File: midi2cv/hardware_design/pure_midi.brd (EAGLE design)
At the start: 78.9 x 100 mm, 92 parts, among them IC1 LD117AS50TR, IC2 74HCT125D, IC3 6N138SMD, IC4 74HCT125D, IC5 STM32F10XCXT6, IC6 LD117AS33TR, J1 CORTEX_DEBUG_PTH, SW1 EC12E_SW, U1 AD5676ARUZ, U2 AD5754BREZ, U3 TEXAS_INSTRUMENTS_LM4040C5IDB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, U4 MAX3421, U5 TEXAS_INSTRUMENTS_LM4040C25ID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, X1 OG-MIDI_MAB5SHCUI-SD-50BV, X2 KUSBVX, X3 OG-MIDI_MAB5SHCUI-SD-50BV, X4 KUSBVX-BS1N, X6 ABRACON_ABM3B-12.000MHZ-B2-TA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, X7 ABRACON_ABM3B-8.000MHZ-B2-TAB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

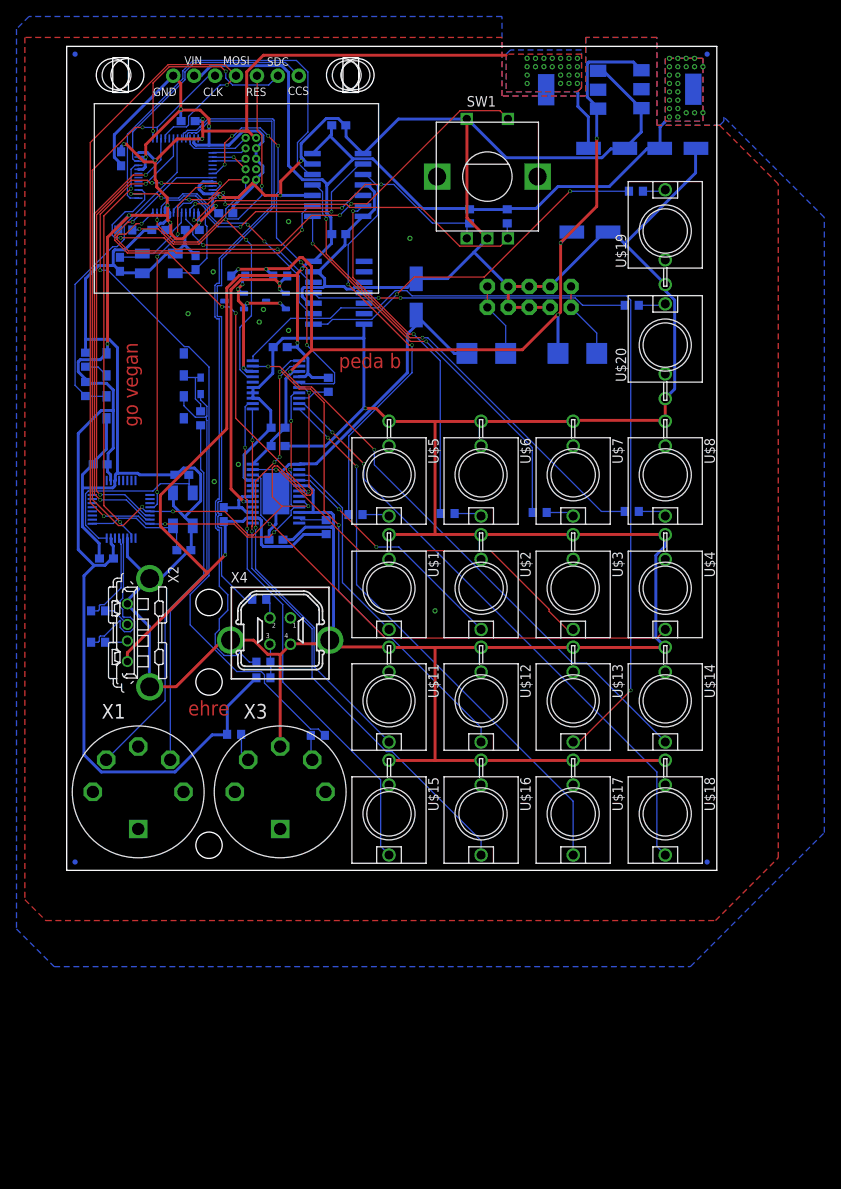
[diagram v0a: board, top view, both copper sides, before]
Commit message: Use newer processor for midi2cv, fix some hardware mistakes
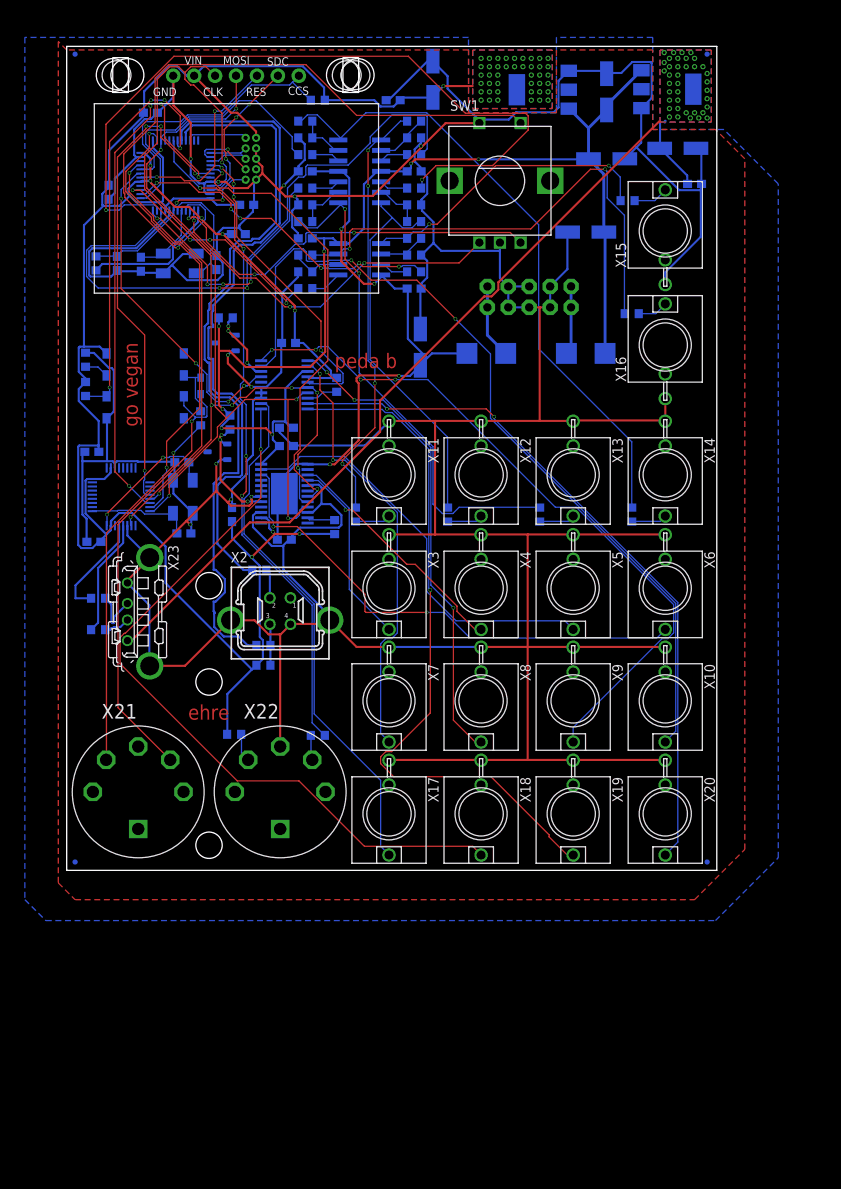
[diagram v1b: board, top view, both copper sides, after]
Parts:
- removed DI1: OLED_1.3_128X64_SPI, microbuilder:C1_ADAFRUIT_1.3_128X64_OLED
- removed U$1, U$11, U$2, U$4: WQP-PJ301M-12_JACK, thonkiconn:WQP-PJ301M-12_JACK
- removed U5: TEXAS_INSTRUMENTS_LM4040C25IDBZRTEXAS_INSTRUMENTS_LM4040C25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, lm4040:TEXAS_INSTRUMENTS_LM4040C25IDBZR_1
- added C18, C19, C20, C22: 22u, GMSN:153CLV-0505
- added C27, C28: 100n, rcl:C0603
- added D4: 1N4001, GMSN:SMADIODE
- added IC7: LD117AS50TR, v-reg:SOT223
- added R22: 33R, rcl:R0603
- added R23, R30, R34, R38: 10k, rcl:R0603
- added R24, R31, R35, R39: 56k, rcl:R0603
- added R25, R28, R32, R36, R40: 39k, rcl:R0603
- added R29, R33, R37: 1k, rcl:R0603
- added X21, X22: OG-MIDI_MAB5SHCUI-SD-50BV, yarns_v03:OG-MIDI_SD-50BV
- added X23: KUSBVX, con-kycon:KUSBVX
- added X24: ABRACON_ABM3B-12.000MHZ-B2-TABRACON_ABM3B-12.000MHZ-B2-T_0_0, Abracon - ABM3B-12.000MHZ-B2-T:ABRACON_ABM3B-12.000MHZ-B2-T_0
- C1, C2, C7, C8: value 22p -> 100n
- C14, C15: value 100n -> 22p
- C21, C23: value 100n -> 22u; device rcl:C0603 -> GMSN:153CLV-0505
- C24, C25: value 100n -> 100nF
- C3, C4: value 22u -> 22p; device GMSN:153CLV-0505 -> rcl:C0603
- C5, C6: value 22u -> 100n; device GMSN:153CLV-0505 -> rcl:C0603
- D1: value 1N4148 -> OLED_1.3_128X64_SPI; device adafruit:SOD-323F -> microbuilder:C1_ADAFRUIT_1.3_128X64_OLED
- D2: value 1N4001 -> 1N4148; device GMSN:SMADIODE -> adafruit:SOD-323F
- IC1: value LD117AS50TR -> STM32F373C; device v-reg:SOT223 -> og-stm32f2:LQFP48
- IC2: value 74HCT125D -> AD5754BREZ; device 74xx-eu:SO14 -> ad5754:RE_24
- IC3: value 6N138SMD -> TL074D; device 6n138:SO8-GW300 -> linear:SO14
- IC4: value 74HCT125D -> TL072D; device 74xx-eu:SO14 -> linear:SO08
- IC5: value STM32F10XCXT6 -> 6N138SMD; device stm32:TQFP48 -> 6n138:SO8-GW300
- R1: value 1k -> 1k5
- R10: value 51R -> 1k
- R11: value 220R -> 1k
- R12: value 470R -> 10k
- R13: value 22R -> 56k
- R14: value 22R -> 39k
- R15: value 10k -> 1k; device resistor:R0603 -> rcl:R0603
- R16: value 10k -> 51R; device resistor:R0603 -> rcl:R0603
- R17: value 1k -> 220R
- R18: value 2k -> 51R
- R19: value 2k -> 1k
- R2, R3: value 4k7 -> 22R
- R20: value 1k5 -> 470R
- R21: value 10k -> 33R
- R26: value 33R -> 10k
- R27: value 33R -> 56k
- R4: value 1k -> 10k
- R5: value 1k -> 10k; device rcl:R0603 -> resistor:R0603
- R6, R7: value 1k -> 4k7
- R8: value 1k -> 2k
- R9: value 51R -> 2k
- U1: value AD5676ARUZ -> TEXAS_INSTRUMENTS_LM4040C5IDBZR1; device AD5676ARUZ:RU_20 -> lm4040:TEXAS_INSTRUMENTS_LM4040C5IDBZR_1
- U2: value AD5754BREZ -> AD5676ARUZ; device ad5754:RE_24 -> AD5676ARUZ:RU_20
- U3: value TEXAS_INSTRUMENTS_LM4040C5IDBZR1 -> TEXAS_INSTRUMENTS_LM4040C25IDBZRTEXAS_INSTRUMENTS_LM4040C25IDBZR_0_1; device lm4040:TEXAS_INSTRUMENTS_LM4040C5IDBZR_1 -> lm4040:TEXAS_INSTRUMENTS_LM4040C25IDBZR_1
- X1: value OG-MIDI_MAB5SHCUI-SD-50BV -> ABRACON_ABM3B-8.000MHZ-B2-TABRACON_ABM3B-8.000MHZ-B2-T_0_0; device yarns_v03:OG-MIDI_SD-50BV -> Abracon - ABM3B-8.000MHZ-B2-T:ABRACON_ABM3B-8.000MHZ-B2-T_0
- X2: value KUSBVX -> KUSBVX-BS1N; device con-kycon:KUSBVX -> con-kycon:KUSBVX-BS1N
- X3: value OG-MIDI_MAB5SHCUI-SD-50BV -> WQP-PJ301M-12_JACK; device yarns_v03:OG-MIDI_SD-50BV -> thonkiconn:WQP-PJ301M-12_JACK
- X4: value KUSBVX-BS1N -> WQP-PJ301M-12_JACK; device con-kycon:KUSBVX-BS1N -> thonkiconn:WQP-PJ301M-12_JACK
- X6: value ABRACON_ABM3B-12.000MHZ-B2-TABRACON_ABM3B-12.000MHZ-B2-T_0_0 -> WQP-PJ301M-12_JACK; device Abracon - ABM3B-12.000MHZ-B2-T:ABRACON_ABM3B-12.000MHZ-B2-T_0 -> thonkiconn:WQP-PJ301M-12_JACK
- X7: value ABRACON_ABM3B-8.000MHZ-B2-TABRACON_ABM3B-8.000MHZ-B2-T_0_0 -> WQP-PJ301M-12_JACK; device Abracon - ABM3B-8.000MHZ-B2-T:ABRACON_ABM3B-8.000MHZ-B2-T_0 -> thonkiconn:WQP-PJ301M-12_JACK
- moved C21 79.9 mm to (74.2, 87.6)
- moved R16 67.1 mm to (30.5, 16.4), turned to 0 degrees
- moved X1 64.3 mm to (13.7, 73.7), flipped to the bottom, turned to 180 degrees
- moved C5 64.2 mm to (10.2, 91.9), turned to 180 degrees
- moved C6 61.1 mm to (6.10, 73.7), turned to 270 degrees
- moved IC1 60.6 mm to (13.2, 84.3), turned to 0 degrees
- moved R26 60.6 mm to (29.0, 82.8)
- moved X7 60.0 mm to (39.1, 20.6), flipped to the top
- moved X6 59.3 mm to (72.6, 34.2), flipped to the top, turned to 180 degrees
- moved R14 58.4 mm to (42.2, 80.8), turned to 180 degrees
- moved C24 57.0 mm to (76.2, 83.3)
- moved R5 56.8 mm to (30.5, 93.5), turned to 180 degrees
- moved R18 55.9 mm to (20.3, 16.5)
- moved C3 54.6 mm to (9.00, 73.6), turned to 90 degrees
- moved R27 53.5 mm to (29.0, 78.7), turned to 180 degrees
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- renumbered U$12 to X8, U$13 to X9, U$14 to X10, U$15 to X17, U$16 to X18, U$17 to X19, U$18 to X20, U$19 to X15, U$20 to X16, U$3 to X5, U$5 to X11, U$6 to X12, U$7 to X13, U$8 to X14
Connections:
- removed net GATE_OUT_5: R7.1, X15.P$1
- new net N$16: IC3.2, R24.2, R25.1
- new net N$24: IC3.10, R26.1
- new net N$25: IC3.3, R23.1
- new net N$26: IC3.14, R29.2, R31.1
- new net N$27: IC3.13, R31.2, R32.1
- new net N$28: IC3.12, R30.1
- new net N$29: IC4.1, R33.2, R35.1
- new net N$30: IC4.2, R35.2, R36.1
- new net N$31: IC4.3, R34.1
- new net N$32: IC4.7, R37.2, R39.1
- new net N$33: IC4.6, R39.2, R40.1
- new net N$34: IC4.5, R38.1
- new net N$35: R33.1, X15.P$1
- new net RST_DAC0: IC1.19, U2.17
- new net RST_OLED: D1.RES, IC1.18
- net +12V: now also C10.1, C12.1, C18.+, C22.+, C23.+, C26.1, C9.1, D3.C, IC2.24, IC3.4, IC4.8, IC7.3, R8.2, R9.2, U2.3; no longer C11.1, C13.1, C3.+, D2.C, IC1.3, R18.2, R19.2, U1.3, U2.24
- net +3V3: now also C1.1, C17.1, C2.1, C20.+, C28.1, C5.1, C7.1, C8.1, D1.VIN, IC1.1, IC1.17, IC1.24, IC1.25, IC1.48, IC1.9, IC2.14, IC5.8, R1.1, R18.2, R20.2, R4.2, R5.2, R6.2, R7.2, U2.4; no longer C14.1, C15.1, C21.1, C23.1, C24.1, C6.+, IC3.8, IC5.1, IC5.24, IC5.36, IC5.48, IC5.9, R10.2, R12.2, R20.1, R21.2
- net +5V: now also C21.+, C24.1, IC7.4, X23.1; no longer C10.1, C12.1, C17.1, C5.+, C9.1, DI1.VIN, IC1.4, IC2.14, IC4.14, R15.2, R16.2, R2.2, R3.2, U1.4, U2.14, X2.1
- net -12V: now also C11.2, C13.2, C19.-, C27.2, D4.A, IC2.1, IC2.25, IC3.11, IC4.4; no longer C26.2, C4.-, D3.A, U2.1, U2.25
- net AREF_25: now also IC2.17, R9.1, U3.1; no longer R18.1, U2.17, U5.1
- net AREF_5: now also R8.1, U1.1, U2.18; no longer R19.1, U1.18, U3.1
- net CV_OUT_1: now also IC2.3, X3.P$1; no longer U$1.P$1, U2.3
- net CV_OUT_10: now also U2.11; no longer U1.11
- net CV_OUT_11: now also U2.10; no longer U1.10
- net CV_OUT_12: now also U2.9; no longer U1.9
- net CV_OUT_2: now also IC2.4, X4.P$1; no longer U$2.P$1, U2.4
- net CV_OUT_3: now also IC2.23; no longer U2.23
- net CV_OUT_4: now also IC2.22, X6.P$1; no longer U$4.P$1, U2.22
- net CV_OUT_5: now also U2.2, X7.P$1; no longer U$11.P$1, U1.2
- net CV_OUT_6: now also U2.1; no longer U1.1
- net CV_OUT_7: now also U2.20; no longer U1.20
- net CV_OUT_8: now also U2.19; no longer U1.19
- net CV_OUT_9: now also U2.12; no longer U1.12
- net D_GATE_OUT_1: now also IC1.10, R23.2; no longer IC2.2, IC5.10
- net D_GATE_OUT_2: now also IC1.11, R12.2; no longer IC2.5, IC5.11
- net D_GATE_OUT_3: now also IC1.12, R26.2; no longer IC2.9, IC5.12
- net D_GATE_OUT_4: now also IC1.13, R30.2; no longer IC2.12, IC5.13
- net D_GATE_OUT_5: now also IC1.14, R34.2; no longer IC4.9, IC5.14
- net D_GATE_OUT_6: now also IC1.15, R38.2; no longer IC4.12, IC5.15
- net ENC_A: now also IC1.2; no longer IC5.2, R15.1
- net ENC_B: now also IC1.3; no longer IC5.3, R16.1
- net ENC_SW: now also IC1.4; no longer IC5.4
- net GATE_OUT_1: now also R10.1; no longer R1.1
- net GATE_OUT_2: now also R11.1; no longer R4.1
- net GATE_OUT_3: now also R15.1; no longer R5.1
- net GATE_OUT_4: now also R29.1; no longer R6.1
- net GATE_OUT_6: now also R37.1; no longer R8.1
- net GND: now also C1.2, C11.1, C13.1, C14.1, C15.1, C18.-, C19.+, C2.2, C20.-, C21.-, C22.-, C23.-, C26.2, C27.1, C28.2, C3.1, C4.1, C5.2, C6.2, C7.2, C8.2, D1.GND, IC1.23, IC1.44, IC1.47, IC1.8, IC2.15, IC2.18, IC2.19, IC2.20, IC2.21, IC2.5, IC5.5, IC7.1, R14.2, R19.1, R25.2, R28.2, R32.2, R36.2, R40.2, U1.2, U2.13, U2.14, X1.2, X1.4, X22.2, X23.4, X23.M1, X23.M2, X24.2, X24.4, X3.P$3, X4.P$3, X6.P$3, X7.P$3; no longer C1.1, C11.2, C13.2, C14.2, C15.2, C2.1, C21.2, C23.2, C26.1, C3.-, C4.+, C5.-, C6.-, C7.1, C8.1, DI1.GND, IC1.1, IC2.1, IC2.13, IC2.4, IC2.7, IC3.5, IC4.10, IC4.13, IC4.7, IC5.20, IC5.23, IC5.35, IC5.44, IC5.47, IC5.8, R17.1, U$1.P$3, U$11.P$3, U$2.P$3, U$4.P$3, U1.13, U1.14, U1.15, U2.10, U2.18, U2.19, U2.20, U2.21, U2.5, U5.2, X3.2, X4.4, X4.M1, X4.M2, X6.2, X6.4, X7.2, X7.4
- net INT_USB: now also IC1.21; no longer IC5.21
- net JTCK: now also IC1.37; no longer IC5.37
- net JTDI: now also IC1.38; no longer IC5.38
- net JTDO: now also IC1.39; no longer IC5.39
- net JTMS: now also IC1.34; no longer IC5.34
- net MIDI_DATA_IN: now also IC1.31, IC5.6, R20.1; no longer IC3.6, IC5.31, R12.1
- net MIDI_DATA_OUT: now also IC1.30, R16.1; no longer IC5.30, R9.1
- net MISO: now also IC1.26; no longer IC5.27
- net MOSI: now also D1.MOSI, IC1.27, IC2.9, U2.7; no longer DI1.MOSI, IC5.28, U1.7, U2.9
- net N$1: now also R7.1, U2.8; no longer R2.1, U1.8
- net N$10: now also IC3.1, R10.2, R24.1; no longer IC2.3, R1.2
- net N$11: now also IC3.7, R11.2, R13.1; no longer IC2.6, R4.2
- net N$12: now also IC5.7, R19.2; no longer IC3.7, R17.2
- net N$13: now also D3.A; no longer D2.A
- net N$14: now also IC3.6, R13.2, R14.1; no longer IC2.8, R5.2
- net N$15: now also IC3.5, R12.1; no longer IC2.11, R6.2
- net N$17: now also IC3.8, R15.2, R27.1; no longer IC4.8, R7.2
- net N$18: now also IC3.9, R27.2, R28.1; no longer IC4.11, R8.2
- net N$19: now also R16.2, X22.5; no longer R9.2, X3.5
- net N$2: now also IC2.11, R6.1; no longer R3.1, U2.11
- net N$20: now also D4.C; no longer D3.C
- net N$21: now also R2.1, X2.2; no longer R13.1, X4.2
- net N$22: now also R18.1, X22.4; no longer R10.1, X3.4
- net N$23: now also R1.2, R3.1, X2.3; no longer R14.1, R20.2, X4.3
- net N$3: now also C4.2, IC1.6, X1.3; no longer C2.2, IC5.6, X7.3
- net N$4: now also D2.C, IC5.2, R17.2; no longer D1.C, IC3.2, R11.2
- net N$5: now also R17.1, X21.4; no longer R11.1, X1.4
- net N$6: now also C3.2, IC1.5, X1.1; no longer C1.2, IC5.5, X7.1
- net N$7: now also C14.2, X24.1; no longer C8.2, X6.1
- net N$8: now also C15.2, X24.3; no longer C7.2, X6.3
- net N$9: now also D2.A, IC5.3, X21.5; no longer D1.A, IC3.3, X1.5
- net RST: now also C6.1, IC1.7, R4.1; no longer DI1.RES, IC5.7, R21.1, U1.17
- net RST_USB: now also IC1.42; no longer IC5.45
- net SCK: now also D1.CLK, IC1.45, IC2.8, U2.6; no longer DI1.CLK, IC5.26, U1.6, U2.8
- net SDC_OLED: now also D1.SDC, IC1.46; no longer DI1.SDC, IC5.25
- net SS_DAC0: now also IC1.40, U2.5; no longer IC5.42, U1.5
- net SS_DAC1: now also IC1.41, IC2.7; no longer IC5.43, U2.7
- net SS_OLED: now also D1.CCS, IC1.20, R5.1; no longer DI1.CCS, IC5.22
- net SS_USB: now also IC1.43; no longer IC5.46
- net USB_D_N: now also R22.1, X23.2; no longer R26.1, X2.2
- net USB_D_P: now also R21.1, X23.3; no longer R27.1, X2.3
- net USB_N: now also R22.2; no longer R26.2
- net USB_P: now also R21.2; no longer R27.2
- net USB_PER_D_N: now also IC1.32, R2.2; no longer IC5.32, R13.2
- net USB_PER_D_P: now also IC1.33, R3.2; no longer IC5.33, R14.2
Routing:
- net +5V: track 207.4 -> 102.6 mm, vias 27 -> 38
- net +3V3: track 223.1 -> 305.8 mm, vias 32 -> 51
- net N$26: track 0.00 -> 77.3 mm
- net D_GATE_OUT_2: track 29.7 -> 93.2 mm
- net N$32: track 0.00 -> 59.6 mm, vias 0 -> 2
- net N$15: track 58.5 -> 3.47 mm, vias 2 -> 0
- net RST: track 72.2 -> 23.5 mm, vias 5 -> 2
- net D_GATE_OUT_1: track 32.5 -> 75.8 mm
- net N$14: track 48.2 -> 5.88 mm, vias 2 -> 0
- net RST_DAC0: track 0.00 -> 40.4 mm, vias 0 -> 4
- net N$29: track 0.00 -> 36.4 mm, vias 0 -> 2
- net ENC_SW: track 49.0 -> 82.2 mm, vias 3 -> 1
- net CV_OUT_8: track 70.1 -> 103.0 mm
- net -12V: track 45.0 -> 77.7 mm, vias 0 -> 4
- net N$18: track 38.4 -> 5.90 mm, vias 2 -> 0
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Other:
- board text added: "Pure MIDI v1.1"
- board text removed: "Pure MIDI v1"

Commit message: Use some sweet ass voltage references
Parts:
- removed R8, R9: 2k, rcl:R0603
- removed U1: TEXAS_INSTRUMENTS_LM4040C5IDBZR1, lm4040:TEXAS_INSTRUMENTS_LM4040C5IDBZR_1
- removed U3: TEXAS_INSTRUMENTS_LM4040C25IDBZRTEXAS_INSTRUMENTS_LM4040C25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, lm4040:TEXAS_INSTRUMENTS_LM4040C25IDBZR_1
- added C29, C30, C31, C32: 100n, rcl:C0603
- added IC8: ADR435, analog-adr43x:MSOP8
- added IC9: ADR431, analog-adr43x:MSOP8
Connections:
- net +12V: now also C29.1, C30.1, IC8.2, IC9.2; no longer R8.2, R9.2
- net AREF_25: now also C32.1, IC9.6; no longer R9.1, U3.1
- net AREF_5: now also C31.1, IC8.6; no longer R8.1, U1.1
- net GND: now also C29.2, C30.2, C31.2, C32.2, IC8.4, IC9.4; no longer U1.2, U3.2
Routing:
- net MIDI_DATA_OUT: track 81.9 -> 140.5 mm, vias 4 -> 2
- net +5V: track 102.6 -> 155.1 mm, vias 38 -> 39
- net MOSI: track 97.6 -> 132.1 mm, vias 5 -> 4
- net ENC_SW: track 82.2 -> 49.3 mm, vias 1 -> 3
- net N$8: track 17.0 -> 43.9 mm
- net SCK: track 113.6 -> 86.9 mm
- net +12V: track 148.8 -> 171.0 mm, vias 7 -> 5
- net N$32: track 59.6 -> 41.5 mm
- net SS_USB: track 65.7 -> 49.5 mm
- net D_GATE_OUT_2: track 93.2 -> 78.8 mm
- net CV_OUT_7: track 85.9 -> 71.8 mm, vias 4 -> 3
- net CV_OUT_10: track 91.5 -> 77.7 mm, vias 1 -> 3
- net ENC_B: track 48.5 -> 62.3 mm, vias 3 -> 1
- net MIDI_DATA_IN: track 50.2 -> 37.3 mm, vias 4 -> 2
- net CV_OUT_9: track 64.0 -> 76.6 mm, vias 0 -> 1
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
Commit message: Last layout improvements
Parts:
- R21, R22: value 33R -> 22R
- R6, R7: value 4k7 -> 10k
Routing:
- net GND: track 717.5 -> 711.0 mm, vias 9 -> 22
- net +12V: track 171.0 -> 170.3 mm
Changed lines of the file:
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@@
 </autorouter>
 <elements>
-<element name="R7" library="rcl" library_urn="urn:adsk.eagle:library:334" package="R0603" package3d_urn="urn:adsk.eagle:package:23555/3" value="4k7" x="32.766" y="58.928" smashed="yes" rot="MR90">
+<element name="R7" library="rcl" library_urn="urn:adsk.eagle:library:334" package="R0603" package3d_urn="urn:adsk.eagle:package:23555/3" value="10k" x="32.766" y="58.928" smashed="yes" rot="MR90">
 <attribute name="NAME" x="33.02" y="54.991" size="1.27" layer="26" rot="MR90"/>
 <attribute name="POPULARITY" value="70" x="32.766" y="58.928" size="1.778" layer="28" rot="MR90" display="off"/>
@@
 <attribute name="VALUE" x="3.1058" y="39.4736" size="1.27" layer="27" rot="R270"/>
 </element>
-<element name="R22" library="rcl" library_urn="urn:adsk.eagle:library:334" package="R0603" package3d_urn="urn:adsk.eagle:package:23555/3" value="33R" x="3.81" y="29.21" smashed="yes" rot="MR0">
+<element name="R22" library="rcl" library_urn="urn:adsk.eagle:library:334" package="R0603" package3d_urn="urn:adsk.eagle:package:23555/3" value="22R" x="3.81" y="29.21" smashed="yes" rot="MR0">
 <attribute name="NAME" x="4.445" y="30.48" size="1.27" layer="26" rot="MR0"/>
 <attribute name="POPULARITY" value="70" x="3.81" y="29.21" size="1.778" layer="28" rot="MR0" display="off"/>
@@
 <attribute name="VALUE" x="4.445" y="26.67" size="1.27" layer="28" rot="MR0"/>
 </element>
-<element name="R21" library="rcl" library_urn="urn:adsk.eagle:library:334" package="R0603" package3d_urn="urn:adsk.eagle:package:23555/3" value="33R" x="3.81" y="33.02" smashed="yes" rot="MR0">
+<element name="R21" library="rcl" library_urn="urn:adsk.eagle:library:334" package="R0603" package3d_urn="urn:adsk.eagle:package:23555/3" value="22R" x="3.81" y="33.02" smashed="yes" rot="MR0">
 <attribute name="NAME" x="4.445" y="34.29" size="1.27" layer="26" rot="MR0"/>
 <attribute name="POPULARITY" value="70" x="3.81" y="33.02" size="1.778" layer="28" rot="MR0" display="off"/>
@@
 <attribute name="VALUE" x="27.051" y="38.227" size="1.27" layer="28" rot="MR0"/>
 </element>
-<element name="R6" library="rcl" library_urn="urn:adsk.eagle:library:334" package="R0603" package3d_urn="urn:adsk.eagle:package:23555/3" value="4k7" x="32.512" y="41.656" smashed="yes" rot="MR270">
+<element name="R6" library="rcl" library_urn="urn:adsk.eagle:library:334" package="R0603" package3d_urn="urn:adsk.eagle:package:23555/3" value="10k" x="32.512" y="41.656" smashed="yes" rot="MR270">
 <attribute name="NAME" x="32.893" y="39.751" size="1.27" layer="26" rot="MR270"/>
 <attribute name="POPULARITY" value="70" x="32.512" y="41.656" size="1.778" layer="28" rot="MR270" display="off"/>
@@
 <contactref element="C13" pad="1"/>
 <contactref element="C28" pad="2"/>
-<wire x1="65.532" y1="96.7105" x2="65.532" y2="96.688" width="0.254" layer="16"/>
-<wire x1="69.723" y1="92.456" x2="69.748" y2="92.5055" width="0.254" layer="16"/>
-<wire x1="69.85" y1="92.583" x2="69.748" y2="92.5055" width="0.254" layer="16"/>
 <contactref element="IC8" pad="4"/>
 <contactref element="IC9" pad="4"/>
@@
 <wire x1="65.43675" y1="96.774" x2="65.24625" y2="96.9645" width="0.3048" layer="16"/>
 <wire x1="60.96" y1="96.9645" x2="60.935" y2="97.042" width="0.3048" layer="16"/>
-<wire x1="65.43675" y1="96.774" x2="65.532" y2="96.688" width="0.3048" layer="16"/>
-<wire x1="65.62725" y1="96.67875" x2="69.723" y2="92.583" width="0.3048" layer="16"/>
-<wire x1="69.723" y1="92.583" x2="69.748" y2="92.5055" width="0.3048" layer="16"/>
-<wire x1="65.62725" y1="96.67875" x2="65.532" y2="96.688" width="0.3048" layer="16"/>
 <wire x1="67.818" y1="90.58275" x2="67.818" y2="86.39175" width="0.3048" layer="16"/>
 <wire x1="69.62775" y1="92.3925" x2="67.818" y2="90.58275" width="0.3048" layer="16"/>
@@
 <wire x1="74.00925" y1="90.01125" x2="72.009" y2="90.01125" width="0.3048" layer="16"/>
 <wire x1="76.29525" y1="87.72525" x2="74.00925" y2="90.01125" width="0.3048" layer="16"/>
-<wire x1="69.723" y1="92.29725" x2="69.748" y2="92.5055" width="0.3048" layer="16"/>
 <wire x1="76.29525" y1="87.72525" x2="76.368" y2="87.63" width="0.3048" layer="16"/>
 <wire x1="50.292" y1="54.483" x2="39.14775" y2="54.483" width="0.3048" layer="1"/>
@@
 <vertex x="48.768" y="101.092"/>
 </polygon>
+<via x="5.08" y="88.9" extent="1-16" drill="0.35"/>
+<via x="4.572" y="92.456" extent="1-16" drill="0.35"/>
+<via x="34.036" y="89.916" extent="1-16" drill="0.35"/>
+<via x="38.608" y="66.548" extent="1-16" drill="0.35"/>
+<via x="44.196" y="68.58" extent="1-16" drill="0.35"/>
+<via x="44.196" y="53.34" extent="1-16" drill="0.35"/>
+<via x="15.24" y="65.024" extent="1-16" drill="0.35"/>
+<via x="16.764" y="68.58" extent="1-16" drill="0.35"/>
+<via x="20.32" y="59.944" extent="1-16" drill="0.35"/>
+<via x="7.62" y="65.532" extent="1-16" drill="0.35"/>
+<via x="10.668" y="68.072" extent="1-16" drill="0.35"/>
+<via x="21.844" y="48.768" extent="1-16" drill="0.35"/>
+<via x="20.574" y="46.7995" extent="1-16" drill="0.35"/>
+<wire x1="4.572" y1="92.456" x2="5.08" y2="88.9" width="0" layer="19" extent="1-1"/>
 </signal>
 <signal name="-12V" class="1">
@@
 <contactref element="IC4" pad="8"/>
 <contactref element="C26" pad="1"/>
-<wire x1="65.532" y1="92.8895" x2="65.532" y2="92.288" width="0.3556" layer="16"/>
-<wire x1="60.978" y1="92.442" x2="60.935" y2="92.442" width="0.3556" layer="16"/>
 <contactref element="IC8" pad="2"/>
 <contactref element="IC9" pad="2"/>

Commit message: Update midi board layout
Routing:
- net GND: track 711.0 -> 706.1 mm, vias 22 -> 37
